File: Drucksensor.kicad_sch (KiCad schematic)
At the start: 58 parts, among them J101 Conn_01x02, J102 Start, J103 RJ45, J104 RJ45, J105 DB15_Female_MountingHoles, J106 Serial, J107 Conn_01x03_Male, Q101 Q_NMOS_GSD, Q102 Q_NMOS_GSD, Q103 Q_NMOS_GSD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

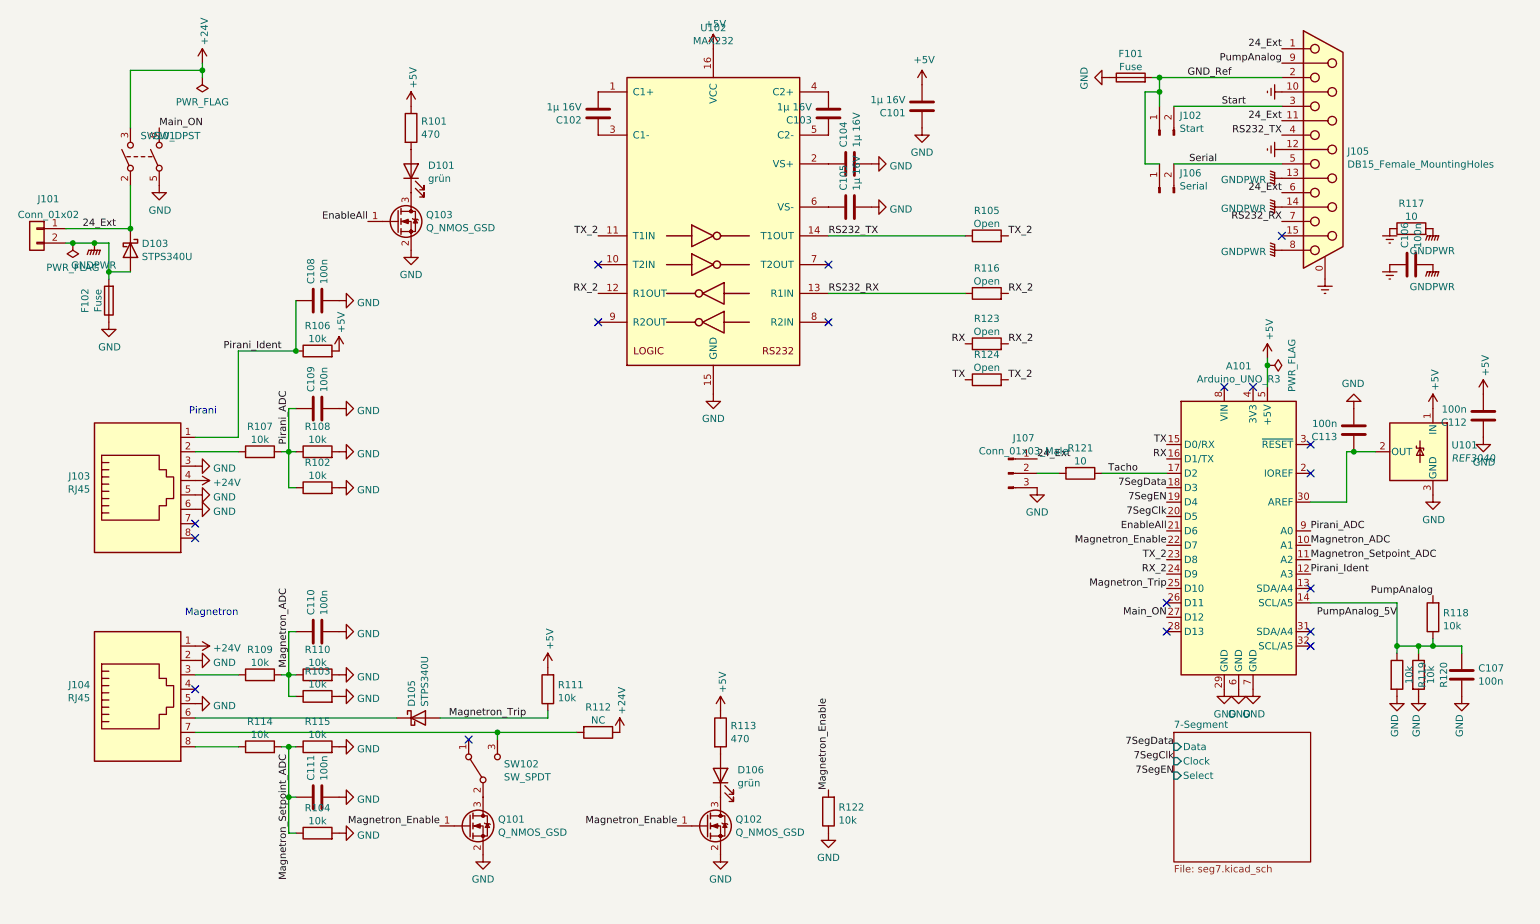
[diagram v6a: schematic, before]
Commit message: Andere Werte für spannungsteiler
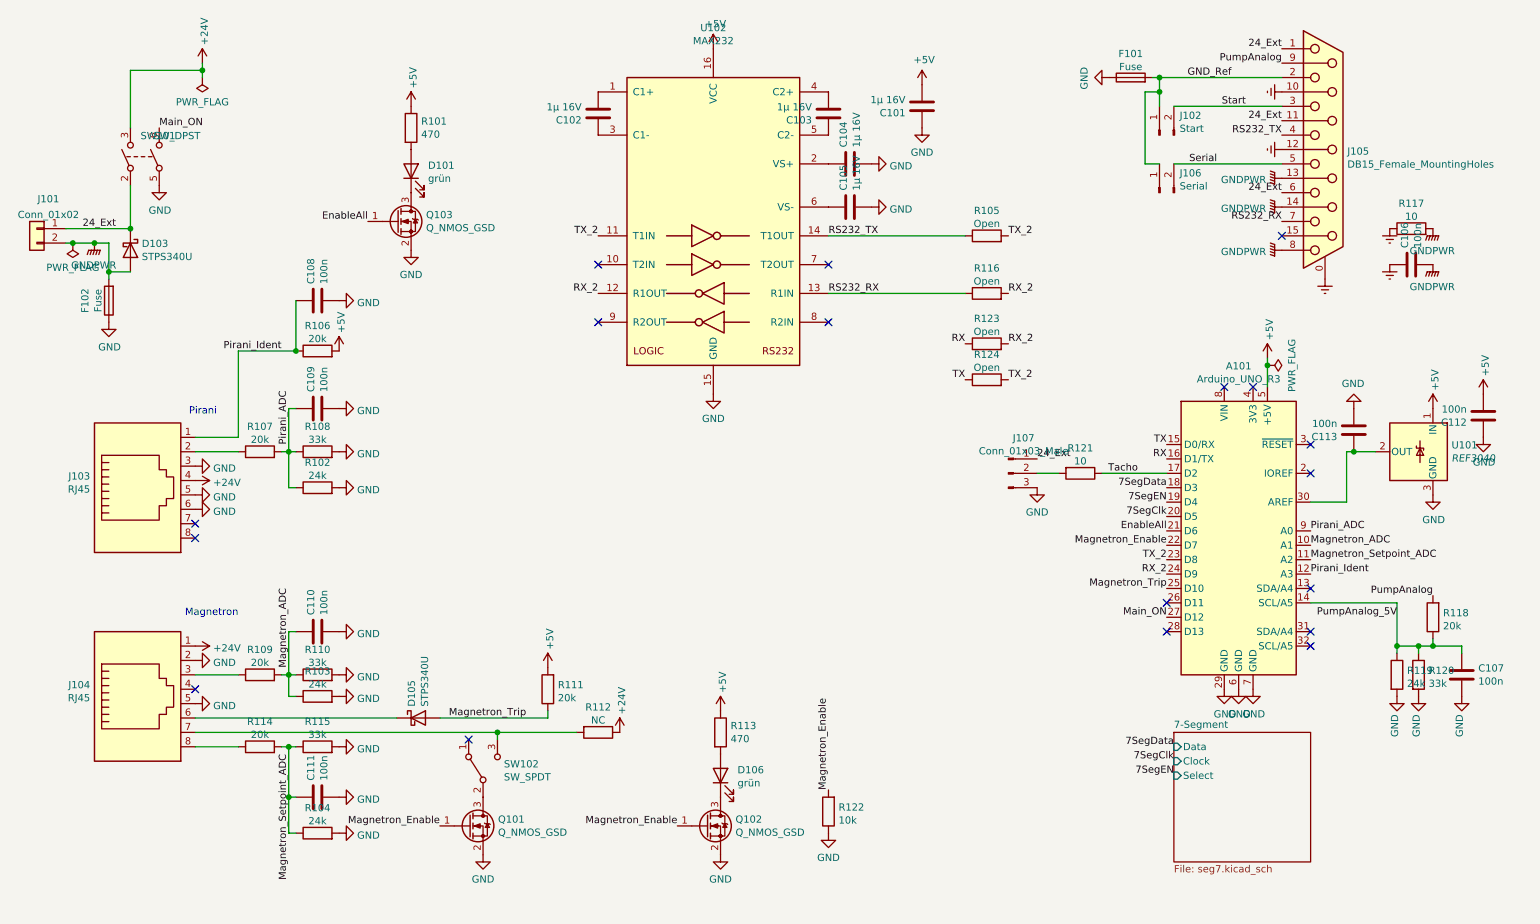
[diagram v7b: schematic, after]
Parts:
- R102, R103, R104, R119: value 10k -> 24k
- R106, R107, R109, R111, R114, R118: value 10k -> 20k
- R108, R110, R115, R120: value 10k -> 33k
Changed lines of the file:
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@@
     (in_bom yes) (on_board yes) (fields_autoplaced)
     (property "Reference" "R107" (id 0) (at 64.77 85.7208 90))
-    (property "Value" "10k" (id 1) (at 64.77 88.0195 90))
+    (property "Value" "20k" (id 1) (at 64.77 88.0195 90))
     (property "Footprint" "Resistor_SMD:R_0603_1608Metric" (id 2) (at 64.77 91.948 90)
       (effects (font (size 1.27 1.27)) hide)
@@
     (in_bom yes) (on_board yes) (fields_autoplaced)
     (property "Reference" "R109" (id 0) (at 64.77 125.0908 90))
-    (property "Value" "10k" (id 1) (at 64.77 127.3895 90))
+    (property "Value" "20k" (id 1) (at 64.77 127.3895 90))
     (property "Footprint" "Resistor_SMD:R_0603_1608Metric" (id 2) (at 64.77 131.318 90)
       (effects (font (size 1.27 1.27)) hide)
@@
     (in_bom yes) (on_board yes) (fields_autoplaced)
     (property "Reference" "R114" (id 0) (at 64.77 137.7908 90))
-    (property "Value" "10k" (id 1) (at 64.77 140.0895 90))
+    (property "Value" "20k" (id 1) (at 64.77 140.0895 90))
     (property "Footprint" "Resistor_SMD:R_0603_1608Metric" (id 2) (at 64.77 144.018 90)
       (effects (font (size 1.27 1.27)) hide)
@@
     (in_bom yes) (on_board yes) (fields_autoplaced)
     (property "Reference" "R106" (id 0) (at 74.93 67.9408 90))
-    (property "Value" "10k" (id 1) (at 74.93 70.2395 90))
+    (property "Value" "20k" (id 1) (at 74.93 70.2395 90))
     (property "Footprint" "Resistor_SMD:R_0603_1608Metric" (id 2) (at 74.93 74.168 90)
       (effects (font (size 1.27 1.27)) hide)
@@
     (in_bom yes) (on_board yes) (fields_autoplaced)
     (property "Reference" "R108" (id 0) (at 74.93 85.7208 90))
-    (property "Value" "10k" (id 1) (at 74.93 88.0195 90))
+    (property "Value" "33k" (id 1) (at 74.93 88.0195 90))
     (property "Footprint" "Resistor_SMD:R_0603_1608Metric" (id 2) (at 74.93 91.948 90)
       (effects (font (size 1.27 1.27)) hide)
@@
     (in_bom yes) (on_board yes) (fields_autoplaced)
     (property "Reference" "R102" (id 0) (at 74.93 92.0708 90))
-    (property "Value" "10k" (id 1) (at 74.93 94.3695 90))
+    (property "Value" "24k" (id 1) (at 74.93 94.3695 90))
     (property "Footprint" "Resistor_SMD:R_0603_1608Metric" (id 2) (at 74.93 98.298 90)
       (effects (font (size 1.27 1.27)) hide)
@@
     (in_bom yes) (on_board yes) (fields_autoplaced)
     (property "Reference" "R110" (id 0) (at 74.93 125.0908 90))
-    (property "Value" "10k" (id 1) (at 74.93 127.3895 90))
+    (property "Value" "33k" (id 1) (at 74.93 127.3895 90))
     (property "Footprint" "Resistor_SMD:R_0603_1608Metric" (id 2) (at 74.93 131.318 90)
       (effects (font (size 1.27 1.27)) hide)
@@
     (in_bom yes) (on_board yes) (fields_autoplaced)
     (property "Reference" "R103" (id 0) (at 74.93 128.9008 90))
-    (property "Value" "10k" (id 1) (at 74.93 131.1995 90))
+    (property "Value" "24k" (id 1) (at 74.93 131.1995 90))
     (property "Footprint" "Resistor_SMD:R_0603_1608Metric" (id 2) (at 74.93 135.128 90)
       (effects (font (size 1.27 1.27)) hide)
@@
     (in_bom yes) (on_board yes) (fields_autoplaced)
     (property "Reference" "R115" (id 0) (at 74.93 137.7908 90))
-    (property "Value" "10k" (id 1) (at 74.93 140.0895 90))
+    (property "Value" "33k" (id 1) (at 74.93 140.0895 90))
     (property "Footprint" "Resistor_SMD:R_0603_1608Metric" (id 2) (at 74.93 144.018 90)
       (effects (font (size 1.27 1.27)) hide)
@@
     (in_bom yes) (on_board yes) (fields_autoplaced)
     (property "Reference" "R104" (id 0) (at 74.93 153.0308 90))
-    (property "Value" "10k" (id 1) (at 74.93 155.3295 90))
+    (property "Value" "24k" (id 1) (at 74.93 155.3295 90))
     (property "Footprint" "Resistor_SMD:R_0603_1608Metric" (id 2) (at 74.93 159.258 90)
       (effects (font (size 1.27 1.27)) hide)
@@
       (effects (font (size 1.27 1.27)) (justify right))
     )
-    (property "Value" "10k" (id 1) (at 117.3481 133.6178 0)
+    (property "Value" "20k" (id 1) (at 117.3481 133.6178 0)
       (effects (font (size 1.27 1.27)) (justify right))
     )
@@
   (symbol (lib_id "Device:R") (at 265.43 129.54 0) (unit 1)
     (in_bom yes) (on_board yes) (fields_autoplaced)
-    (property "Reference" "R119" (id 0) (at 269.8792 129.54 90))
-    (property "Value" "10k" (id 1) (at 267.5805 129.54 90))
+    (property "Reference" "R119" (id 0) (at 267.2081 128.7791 0)
+      (effects (font (size 1.27 1.27)) (justify left))
+    )
+    (property "Value" "24k" (id 1) (at 267.2081 131.0778 0)
+      (effects (font (size 1.27 1.27)) (justify left))
+    )
     (property "Footprint" "Resistor_SMD:R_0603_1608Metric" (id 2) (at 263.652 129.54 90)
       (effects (font (size 1.27 1.27)) hide)
@@
   (symbol (lib_id "Device:R") (at 269.24 129.54 0) (unit 1)
     (in_bom yes) (on_board yes) (fields_autoplaced)
-    (property "Reference" "R120" (id 0) (at 273.6892 129.54 90))
-    (property "Value" "10k" (id 1) (at 271.3905 129.54 90))
+    (property "Reference" "R120" (id 0) (at 271.0181 128.7791 0)
+      (effects (font (size 1.27 1.27)) (justify left))
+    )
+    (property "Value" "33k" (id 1) (at 271.0181 131.0778 0)
+      (effects (font (size 1.27 1.27)) (justify left))
+    )
     (property "Footprint" "Resistor_SMD:R_0603_1608Metric" (id 2) (at 267.462 129.54 90)
       (effects (font (size 1.27 1.27)) hide)
@@
       (effects (font (size 1.27 1.27)) (justify right))
     )
-    (property "Value" "10k" (id 1) (at 273.5581 120.9178 0)
+    (property "Value" "20k" (id 1) (at 273.5581 120.9178 0)
       (effects (font (size 1.27 1.27)) (justify right))
     )
@@
     )
     (path "/46d79db3-8f8c-4aca-a68d-0ba4259d2b25"
-      (reference "R102") (unit 1) (value "10k") (footprint "Resistor_SMD:R_0603_1608Metric")
+      (reference "R102") (unit 1) (value "24k") (footprint "Resistor_SMD:R_0603_1608Metric")
     )
     (path "/0fafd9ed-b4e5-4a31-9141-b309f564e47f"
-      (reference "R103") (unit 1) (value "10k") (footprint "Resistor_SMD:R_0603_1608Metric")
+      (reference "R103") (unit 1) (value "24k") (footprint "Resistor_SMD:R_0603_1608Metric")
     )
     (path "/015fecbc-b937-4354-b975-a92eb0e1747e"
-      (reference "R104") (unit 1) (value "10k") (footprint "Resistor_SMD:R_0603_1608Metric")
+      (reference "R104") (unit 1) (value "24k") (footprint "Resistor_SMD:R_0603_1608Metric")
     )
     (path "/8aa97f47-039b-48c2-9a52-bf1c7afb44c3"
@@
     )
     (path "/5718552a-9e5a-425c-a6b2-49137faa0f65"
-      (reference "R106") (unit 1) (value "10k") (footprint "Resistor_SMD:R_0603_1608Metric")
+      (reference "R106") (unit 1) (value "20k") (footprint "Resistor_SMD:R_0603_1608Metric")
     )
     (path "/89ee89a5-f392-4e46-897b-8c781b752716"
-      (reference "R107") (unit 1) (value "10k") (footprint "Resistor_SMD:R_0603_1608Metric")
+      (reference "R107") (unit 1) (value "20k") (footprint "Resistor_SMD:R_0603_1608Metric")
     )
     (path "/3eb29b0c-b573-42b5-a16e-2149ebe29914"
-      (reference "R108") (unit 1) (value "10k") (footprint "Resistor_SMD:R_0603_1608Metric")
+      (reference "R108") (unit 1) (value "33k") (footprint "Resistor_SMD:R_0603_1608Metric")
     )
     (path "/974300a5-9c70-4dbc-b305-8689fdd183b1"
-      (reference "R109") (unit 1) (value "10k") (footprint "Resistor_SMD:R_0603_1608Metric")
+      (reference "R109") (unit 1) (value "20k") (footprint "Resistor_SMD:R_0603_1608Metric")
     )
     (path "/96328cc7-bb42-489c-9599-10f5a846b77c"
-      (reference "R110") (unit 1) (value "10k") (footprint "Resistor_SMD:R_0603_1608Metric")
+      (reference "R110") (unit 1) (value "33k") (footprint "Resistor_SMD:R_0603_1608Metric")
     )
     (path "/a96b61ea-93bf-43b7-a872-d0d6dec914ea"
-      (reference "R111") (unit 1) (value "10k") (footprint "Resistor_SMD:R_0603_1608Metric")
+      (reference "R111") (unit 1) (value "20k") (footprint "Resistor_SMD:R_0603_1608Metric")
     )
     (path "/9a93970e-1e6d-430e-b6af-e137cae4df9f"
@@
     )
     (path "/113c0353-1f0f-4775-864d-08fd48157a22"
-      (reference "R114") (unit 1) (value "10k") (footprint "Resistor_SMD:R_0603_1608Metric")
+      (reference "R114") (unit 1) (value "20k") (footprint "Resistor_SMD:R_0603_1608Metric")
     )
     (path "/25879add-d912-40a7-932d-33bff4d1b552"
-      (reference "R115") (unit 1) (value "10k") (footprint "Resistor_SMD:R_0603_1608Metric")
+      (reference "R115") (unit 1) (value "33k") (footprint "Resistor_SMD:R_0603_1608Metric")
     )
     (path "/2bfc640d-04ce-4768-bf30-ce244fb32291"
@@
     )
     (path "/3ffff468-3271-4802-bb44-c3ad46d46bb7"
-      (reference "R118") (unit 1) (value "10k") (footprint "Resistor_SMD:R_0603_1608Metric")
+      (reference "R118") (unit 1) (value "20k") (footprint "Resistor_SMD:R_0603_1608Metric")
     )
     (path "/f66dfbf7-1d12-415e-ad5f-19c293bfec52"
-      (reference "R119") (unit 1) (value "10k") (footprint "Resistor_SMD:R_0603_1608Metric")
+      (reference "R119") (unit 1) (value "24k") (footprint "Resistor_SMD:R_0603_1608Metric")
     )
     (path "/599f4e1b-c046-41ac-ab12-29c4a83929bd"
-      (reference "R120") (unit 1) (value "10k") (footprint "Resistor_SMD:R_0603_1608Metric")
+      (reference "R120") (unit 1) (value "33k") (footprint "Resistor_SMD:R_0603_1608Metric")
     )
     (path "/2dbdfdf5-62bc-481a-ab86-cf902a70ae15"
